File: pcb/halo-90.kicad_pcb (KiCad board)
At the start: 4 copper layers, 24 x 24 mm, 102 parts, among them J1 TC2030-SWIM-NL, U1 STM8151G6U6, U2 SC7A20HTR, U3 DRV5032

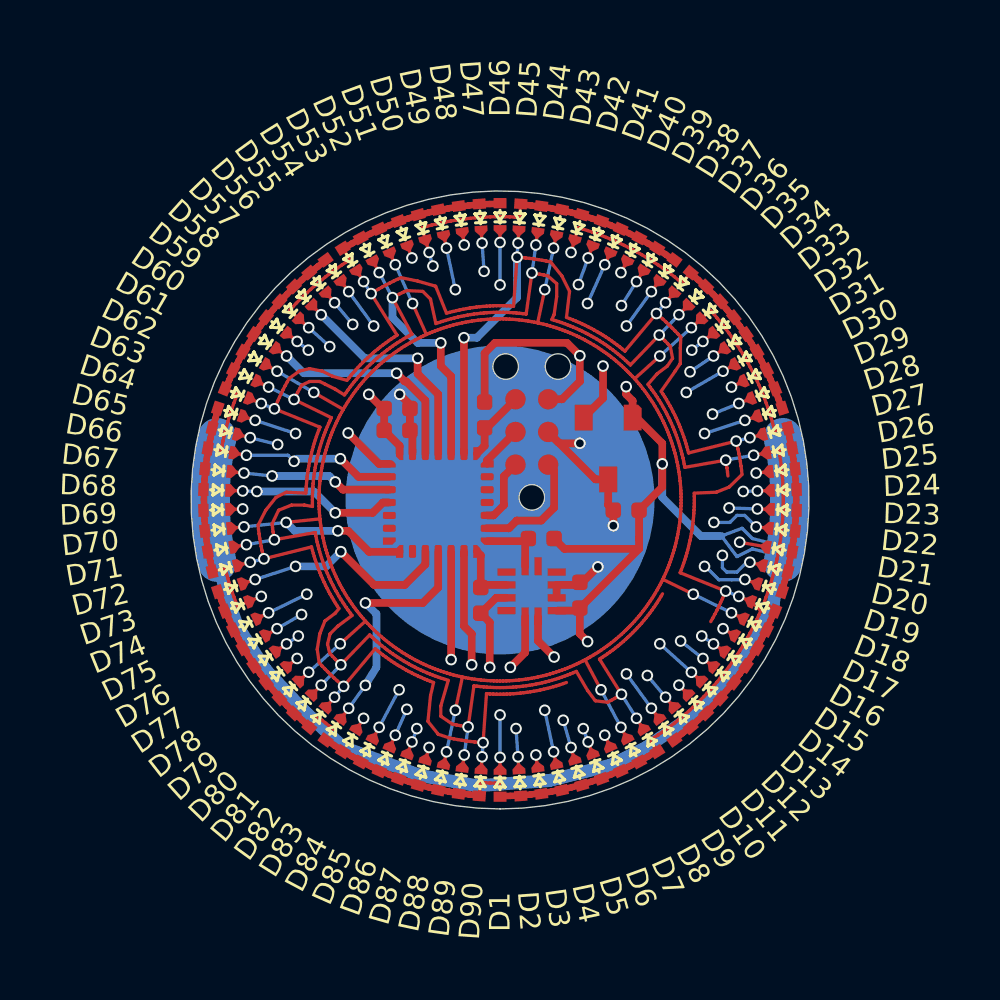
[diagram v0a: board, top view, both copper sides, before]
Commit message: chore(pcb): cleanup components and final manufacturing package regeneration
- Merged manual user footprint updates for SC7A20H, TC2030, tooling holes, and battery
- Regenerated strictly-grouped JLCPCB BOM
- Corrected CPL metric scale
- Removed old/unused component library files
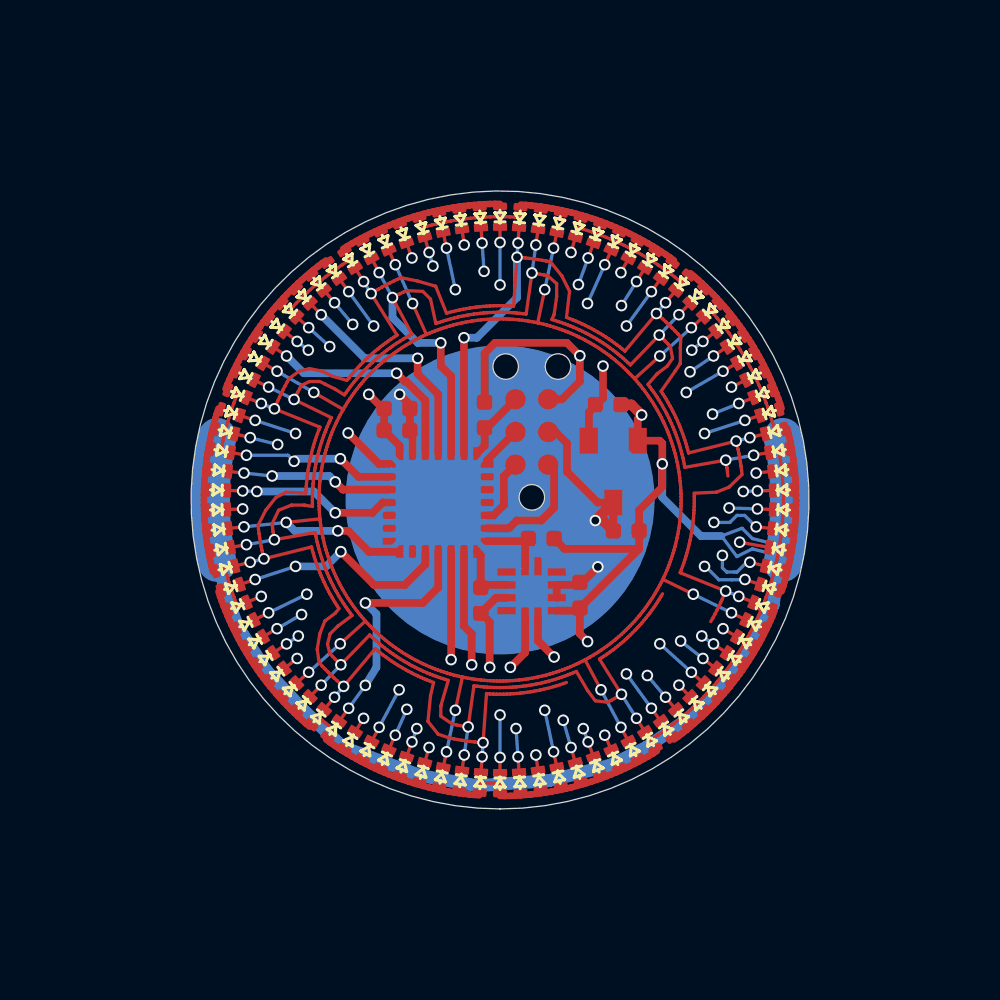
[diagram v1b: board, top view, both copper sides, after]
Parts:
- added R4: 10k, R-0402:R-0402, F.Cu at (4.20, -3.70)
- C1, C2, C3: value 100n -> 100nF
- C4: value 10u -> 10uF
- D1, D10, D11, D12, D13, D14, D15, D16, D17, D18, D19, D2, D20, D21, D22, D23, D24, D25, D26, D27, D28, D29, D3, D30, D31, D32, D33, D34, D35, D36, D37, D38, D39, D4, D40, D41, D42, D43, D44, D45, D46, D47, D48, D49, D5, D50, D51, D52, D53, D54, D55, D56, D57, D58, D59, D6, D60, D61, D62, D63, D64, D65, D66, D67, D68, D69, D7, D70, D71, D72, D73, D74, D75, D76, D77, D78, D79, D8, D80, D81, D82, D83, D84, D85, D86, D87, D88, D89, D9, D90: footprint BL-HUB37A-AV-TRB:D-0402 -> XL-1005SURC:XL-1005SURC
- J1: footprint TC2030-IDC-NL:Tag-Connect_TC2030-IDC-NL_2x03_P1.27mm_Vertical -> TC2030-IDC-NL:TC2030-IDC-NL
- U3: value DRV5032 -> HAL2041SO; footprint DRV5032:DRV5032 -> HAL2041SO:HAL2041SO
- moved U3 0.92 mm to (4.40, -1.10)
- moved C3 0.80 mm to (4.90, 1.20)
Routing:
- net +3V: track 107.0 -> 108.2 mm
- net GND: track 11.3 -> 12.2 mm, vias 4 -> 3
- net HALL: track 15.4 -> 16.2 mm

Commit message: fix(pcb): final LCSC property corrections for BOM generation
- Fixed user manual library edits that assigned the STM8 LCSC to the battery holder and removed it from the MCU
- Regenerated native BOM directly from updated KiCad component properties
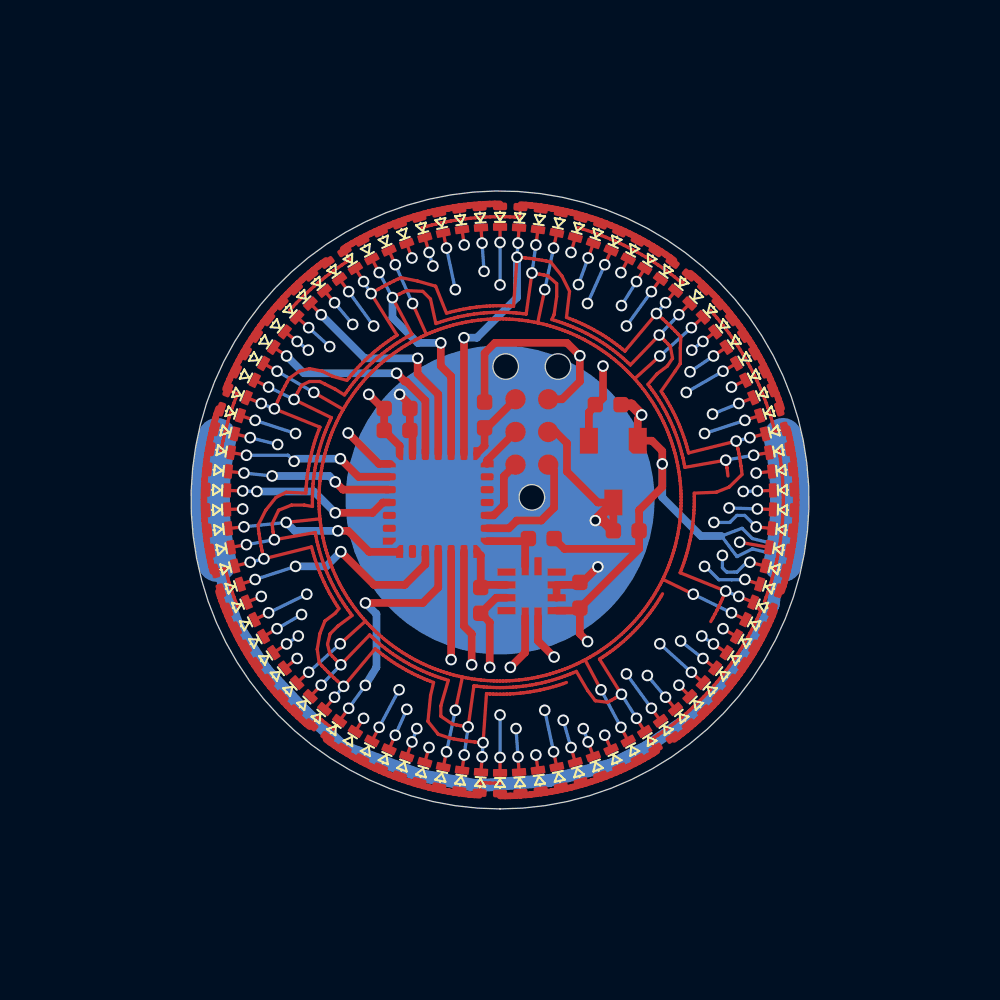
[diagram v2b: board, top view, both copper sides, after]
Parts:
- turned U3 to -90 degrees
